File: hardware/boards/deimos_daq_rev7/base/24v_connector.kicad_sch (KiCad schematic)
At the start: 12 parts, among them IC8001 INA826AIDR, J8001 Barrel_Jack PJ-202BH, U4001 INA181A2

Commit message: add more capacitance on 24V supply
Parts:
- added C5006, C5007, C5008: 10uF 50V 0805, Capacitor_SMD:C_0805_2012Metric, symbol Device:C_Small
- TP4001: now not fitted; now left out of the parts list
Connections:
- net GND: now also C5006.2, C5007.2, C5008.2
- net at C4003.1, J8001.1, R8004.2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: now also C5006.1, C5007.1, C5008.1

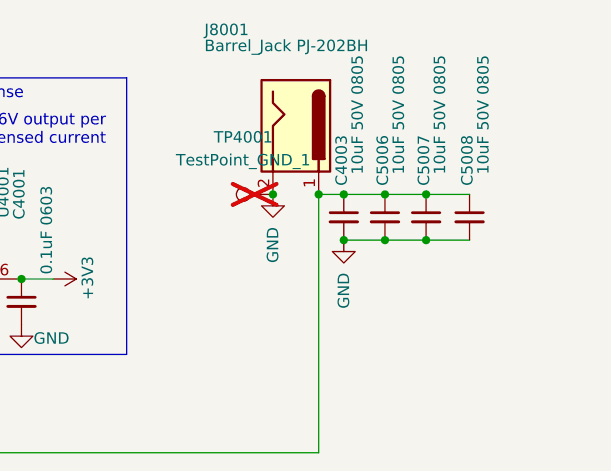
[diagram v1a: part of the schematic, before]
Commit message: Improve power input filters (#67)
* Remove immediate input power caps to eliminate spark on connection
* Add 220nH filter inductors to each converter
* Add LCSC ref number to OPA196 schematic symbols
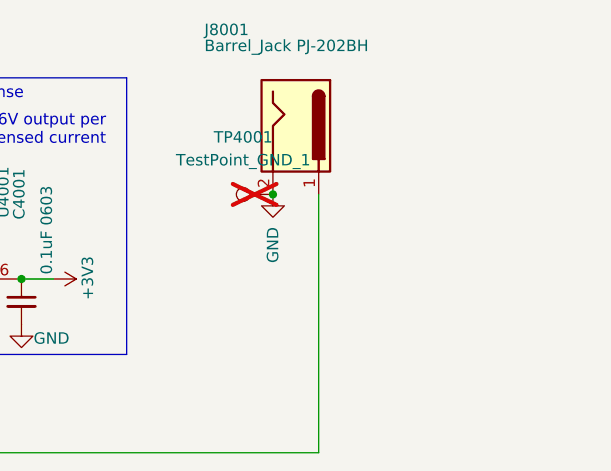
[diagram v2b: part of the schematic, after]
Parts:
- removed C4003, C5006, C5007, C5008: 10uF 50V 0805, Capacitor_SMD:C_0805_2012Metric, symbol Device:C_Small
